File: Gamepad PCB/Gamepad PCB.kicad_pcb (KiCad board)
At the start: 4 copper layers, 136 x 95 mm, 119 parts, among them J1 USB_C_16P, J2 XH2.54, J3 XH2.54, J4 XH2.54, J5 XH2.54, J6 XH2.54, J7 XH2.54, M1 Vibration Motor, Q1 Si2301, Q2 SS8050, Q3 IRF4905, Q4 SS8050, Q5 2N2222, Q6 2N2222, Q7 Si2300, Q8 Si2300, SW1 SW_Push, SW10 Ctrl button, SW11 Config switch, SW12 Corner switch, SW13 Adj button, SW14 Ctrl button, SW15 Config switch, SW16 Corner switch, SW17 Adj button, SW18 Ctrl button, SW19 Config switch, SW2 RST Button, SW3 Boot Button, SW4 Corner button, SW5 Adj button, SW6 Ctrl button, SW7 Config switch, SW8 Corner button, SW9 Adj button, U1 AMS1117-3.3, U10 CP2102, U11 ADS1015IDGS, U12 74HC4051, U13 74HC165D, U2 LC709203FQH-01TWG, U3 USBLC6-2SC6, U4 NRF24L01 PA + LNA, U5 AMS1117-3.3, U6 ESP32-S3-WROOM1, U7 TP4056, U8 DW01A, U9 8205

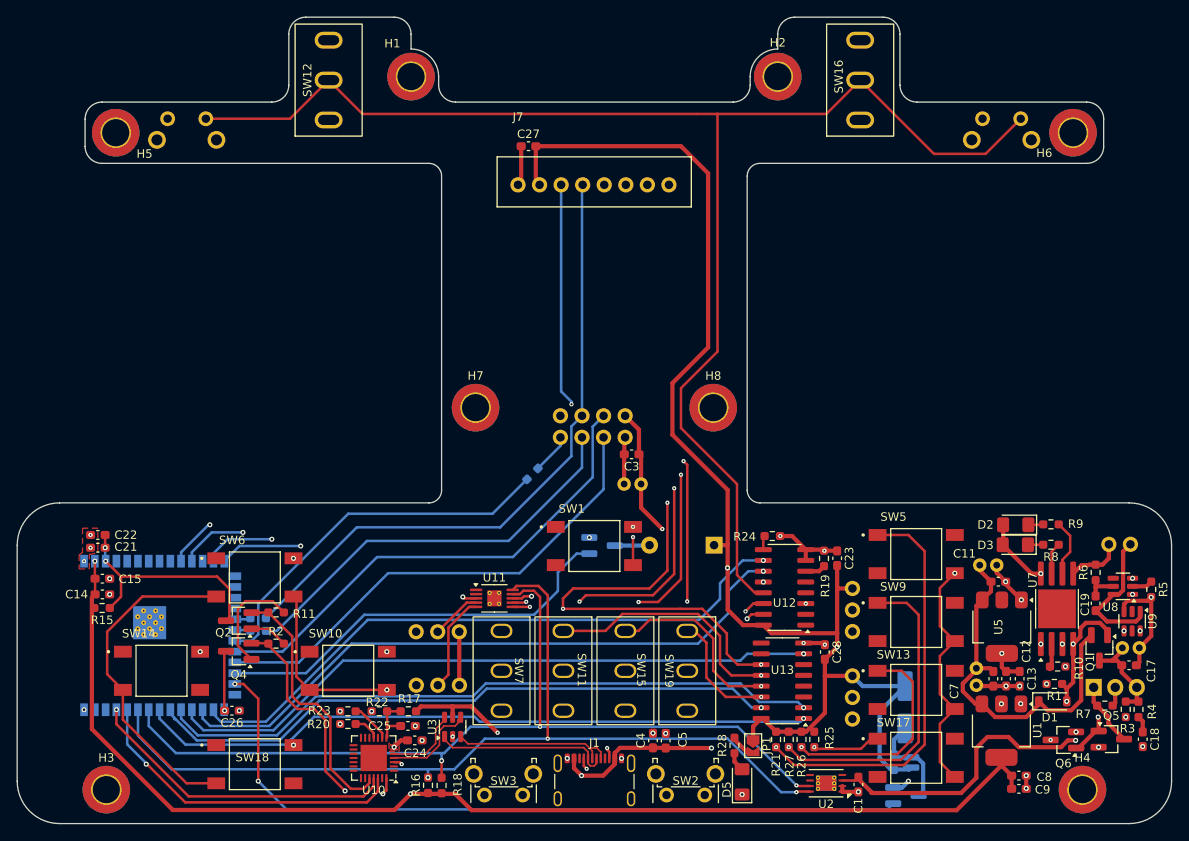
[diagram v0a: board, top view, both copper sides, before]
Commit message: fix entire pcb
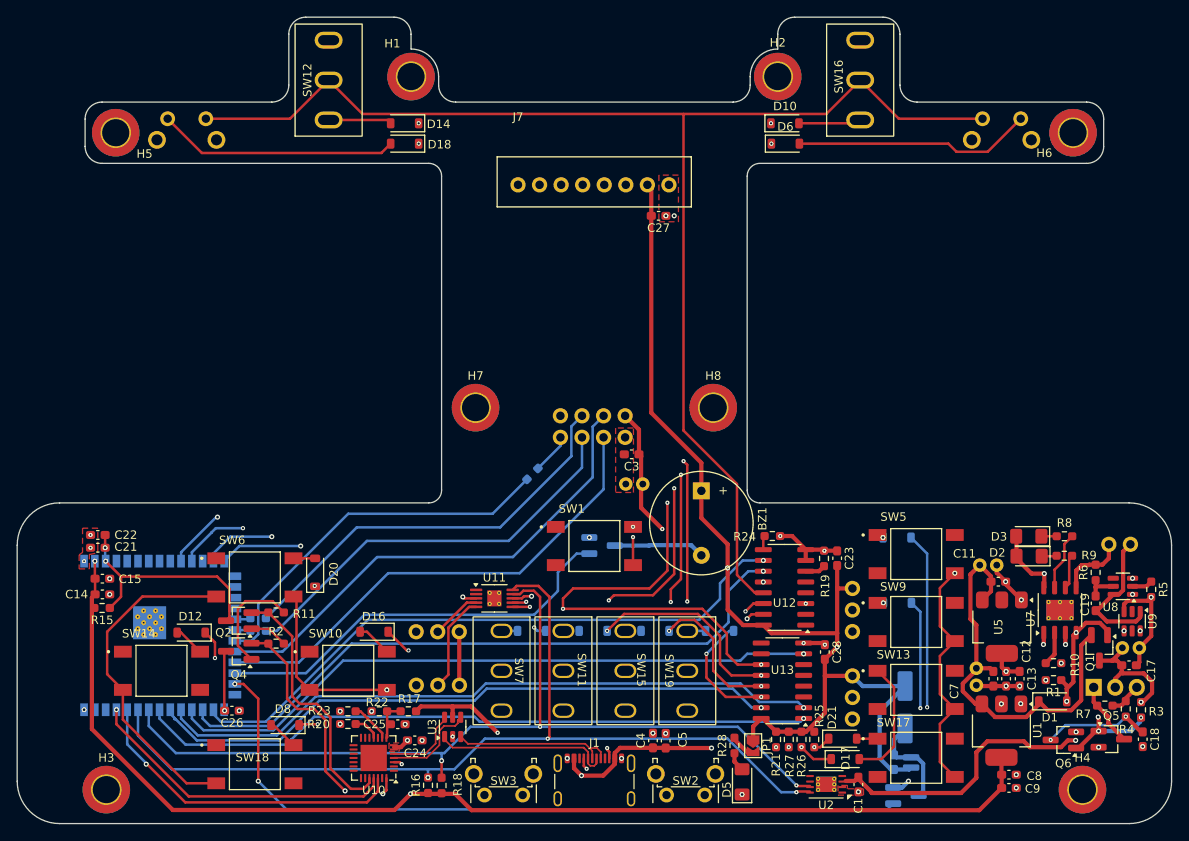
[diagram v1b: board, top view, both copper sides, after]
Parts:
- added D10: 1N4007, Diode_SMD:D_SOD-123, F.Cu at (176.4, 56.5)
- added D11: 1N4007, Diode_SMD:D_SOD-123, B.Cu at (161.2, 116.3)
- added D12: 1N4007, Diode_SMD:D_SOD-123, F.Cu at (106.5, 116.5)
- added D13: 1N4007, Diode_SMD:D_SOD-123, B.Cu at (189.7, 113.0)
- added D14: 1N4007, Diode_SMD:D_SOD-123, F.Cu at (131.7, 56.5)
- added D15: 1N4007, Diode_SMD:D_SOD-123, B.Cu at (153.8, 116.3)
- added D16: 1N4007, Diode_SMD:D_SOD-123, F.Cu at (128.1, 116.4)
- added D17: 1N4007, Diode_SMD:D_SOD-123, F.Cu at (183.6, 131.4)
- added D18: 1N4007, Diode_SMD:D_SOD-123, F.Cu at (131.7, 58.9)
- added D19: 1N4007, Diode_SMD:D_SOD-123, B.Cu at (146.6, 116.3)
- added D20: 1N4007, Diode_SMD:D_SOD-123, F.Cu at (121.1, 109.4)
- added D21: 1N4007, Diode_SMD:D_SOD-123, F.Cu at (183.2, 129.0)
- added D6: 1N4007, Diode_SMD:D_SOD-123, F.Cu at (176.5, 58.9)
- added D7: 1N4007, Diode_SMD:D_SOD-123, B.Cu at (168.8, 116.3)
- added D8: 1N4007, Diode_SMD:D_SOD-123, F.Cu at (117.5, 127.4)
- added D9: 1N4007, Diode_SMD:D_SOD-123, B.Cu at (189.7, 105.3)
- BZ1: moved to F.Cu
- R28: value 1K -> 5.1K
- U7: footprint Package_SO:SOP-8-1EP_4.57x4.57mm_P1.27mm_EP4.57x4.45mm -> Package_SO:HTSOP-8-1EP_3.9x4.9mm_P1.27mm_EP2.4x3.2mm_ThermalVias
- moved C27 17.4 mm to (161.6, 67.4), turned to 180 degrees
- moved BZ1 6.57 mm to (166.6, 99.8), turned to -90 degrees
- moved D2 4.02 mm to (205.2, 107.5)
- moved R9 4.02 mm to (209.4, 107.5)
- moved D3 1.88 mm to (205.2, 105.2)
- moved R8 1.88 mm to (209.4, 105.2)
- moved R3 1.80 mm to (218.4, 125.6)
- moved R4 1.50 mm to (216.6, 125.5)
- moved C25 1.22 mm to (130.8, 127.3)
- moved C9 1.18 mm to (202.8, 134.8)
- moved C8 1.18 mm to (202.8, 133.2)
- moved R10 0.63 mm to (208.1, 120.1)
- moved R1 0.46 mm to (208.1, 122.1)
- moved U7 0.38 mm to (208.8, 113.8)
- moved C2 0.20 mm to (159.7, 99.0)
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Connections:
- J7 pad 1: GND -> /IO17
- J7 pad 2: +3.3V_Perip -> /IO18
- J7 pad 3: /CLK -> /IO19
- J7 pad 4: /MOSI -> /IO20
- J7 pad 5: /IO17 -> /MOSI
- J7 pad 6: /IO18 -> /CLK
- J7 pad 7: /IO19 -> +3.3V_Perip
- J7 pad 8: /IO20 -> GND
- Q3 pad 2: Net-(J2-A) -> +BATT
- Q3 pad 3: +BATT -> Net-(J2-A)
- Q4 pad 3: /GPIO0 -> /IO0
- Q6 pad 3: Net-(Q6-Pad3) -> Net-(C18-Pad1)
- R21 pad 2: Net-(SW19A-A) -> Net-(D6-K)
- R25 pad 2: Net-(SW7A-A) -> Net-(D18-K)
- R26 pad 2: Net-(SW11A-A) -> Net-(D14-K)
- R27 pad 2: Net-(SW15A-A) -> Net-(D10-K)
- R4 pad 1: +BATT -> Net-(J2-A)
- SW1 pad 2: Net-(Q6-Pad3) -> Net-(C18-Pad1)
- SW10 pad 1: Net-(SW11A-A) -> Net-(D16-A)
- SW11 pad 1: Net-(SW11A-A) -> Net-(D15-A)
- SW12 pad 1: Net-(SW11A-A) -> Net-(D14-A)
- SW13 pad 1: Net-(SW11A-A) -> Net-(D17-A)
- SW14 pad 1: Net-(SW15A-A) -> Net-(D12-A)
- SW15 pad 1: Net-(SW15A-A) -> Net-(D11-A)
- SW16 pad 1: Net-(SW15A-A) -> Net-(D10-A)
- SW17 pad 1: Net-(SW7A-A) -> Net-(D21-A)
- SW18 pad 1: Net-(SW19A-A) -> Net-(D8-A)
- SW19 pad 1: Net-(SW19A-A) -> Net-(D7-A)
- SW4 pad 2: Net-(SW7A-A) -> Net-(D18-A)
- SW5 pad 1: Net-(SW19A-A) -> Net-(D9-A)
- SW6 pad 1: Net-(SW7A-A) -> Net-(D20-A)
- SW7 pad 1: Net-(SW7A-A) -> Net-(D19-A)
- SW8 pad 1: Net-(SW12A-B) -> Net-(D6-A)
- SW8 pad 2: Net-(SW19A-A) -> Net-(SW12A-B)
- SW9 pad 1: Net-(SW15A-A) -> Net-(D13-A)
- U13 pad 11: Net-(SW7A-A) -> Net-(D18-K)
- U13 pad 12: Net-(SW11A-A) -> Net-(D14-K)
- U13 pad 13: Net-(SW15A-A) -> Net-(D10-K)
- U13 pad 14: Net-(SW19A-A) -> Net-(D6-K)
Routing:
- net Net-(SW7A-A): track 217.9 -> 0.00 mm, vias 5 -> 0
- net Net-(SW19A-A): track 215.4 -> 0.00 mm, vias 5 -> 0
- net Net-(SW15A-A): track 203.7 -> 0.00 mm, vias 5 -> 0
- net Net-(SW11A-A): track 198.7 -> 0.00 mm, vias 5 -> 0
- net Net-(D6-K): track 0.00 -> 185.8 mm, vias 0 -> 8
- net Net-(D10-K): track 0.00 -> 185.0 mm, vias 0 -> 8
- net Net-(D18-K): track 0.00 -> 176.8 mm, vias 0 -> 7
- net Net-(D14-K): track 0.00 -> 163.3 mm, vias 0 -> 7
- net Net-(C18-Pad1): track 1.94 -> 87.0 mm, vias 0 -> 3
- net Net-(Q6-Pad3): track 74.4 -> 0.00 mm, vias 2 -> 0
- net /GPIO0: track 47.2 -> 0.00 mm, vias 1 -> 0
- net /IO0: track 0.00 -> 46.9 mm, vias 0 -> 1
- net Net-(D18-A): track 0.00 -> 28.4 mm
- net Net-(D6-A): track 0.00 -> 28.1 mm
- net +3.3V_Perip: track 227.2 -> 199.5 mm
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
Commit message: add pcb interface
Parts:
- added C29: 0.1u, Capacitor_SMD:C_0603_1608Metric_Pad1.08x0.95mm_HandSolder, F.Cu at (146.4, 110.0)
- added D22: WS2812B, LED_SMD:LED_WS2812B_PLCC4_5.0x5.0mm_P3.2mm, F.Cu at (131.6, 109.5)
- added D24: Green, Diode_SMD:D_1206_3216Metric_Pad1.42x1.75mm_HandSolder, F.Cu at (146.0, 106.4)
- added R29: 10K, Resistor_SMD:R_0603_1608Metric_Pad0.98x0.95mm_HandSolder, F.Cu at (131.6, 113.3)
- added R30: 5.1K, Resistor_SMD:R_0603_1608Metric_Pad0.98x0.95mm_HandSolder, F.Cu at (142.8, 107.9)
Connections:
- U6 pad 8: unconnected-(U6-IO15-Pad8) -> /RGB_LED
- U6 pad 9: unconnected-(U6-IO16-Pad9) -> /DEFAULT_LED
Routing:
- net /DEFAULT_LED: track 0.00 -> 38.8 mm, vias 0 -> 1
- net /RGB_LED: track 0.00 -> 31.0 mm, vias 0 -> 1
- net +3.3V_Perip: track 199.5 -> 206.1 mm, vias 4 -> 6
- net Net-(D24-A): track 0.00 -> 2.28 mm
- net GND: track 46.7 -> 48.8 mm, vias 46 -> 49
- net +BATT: track 57.7 -> 59.7 mm
- net Net-(D15-A): track 0.00 -> 1.85 mm
- net Net-(D11-A): track 0.00 -> 1.85 mm
- net Net-(D18-K): track 176.8 -> 175.7 mm
